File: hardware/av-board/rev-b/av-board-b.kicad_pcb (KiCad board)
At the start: 4 copper layers, 94.6 x 69.4 mm, 234 parts, among them J1 RCA Y, J10 2x20 socket, J11 XIAO 5V..D7, J12 XIAO D0..D6, J13 SPDIF, J2 RCA Pb, J3 RCA Pr, J4 RCA L, J5 RCA R, J6 HDMI-001, J7 SYNC, J8 VGA, J9 2x20 socket, Q1 2N7002, Q2 2N7002, SW1 TS-1187A-B-A-B, SW2 TS-1187A-B-A-B, U1 ADV7181DBCPZ-RL, U10 TPD4E05U06DQAR, U12 TPS7A2045PDBVR, U13 SN74LVC1GU04DBVR, U14 SN74LVC1G04DBVR, U15 SN74LVC1G04DBVR, U19 TPD4E05U06DQAR, U2 ADV7511KSTZ, U20 TPD4E05U06DQAR, U21 SN74LVC2G17DBVR, U22 SN74LVC8T245PWR, U23 SN74AVC4T245PWR, U3 PCM1808PWR, U4 TLV62569DBVR, U5 TPS7A7001DDAR, U6 TPS7A7001DDAR, U7 TPS7A7001DDAR, U8 TPD4E05U06DQAR, U9 TPD4E05U06DQAR, Y1 28.63636MHz 20pF

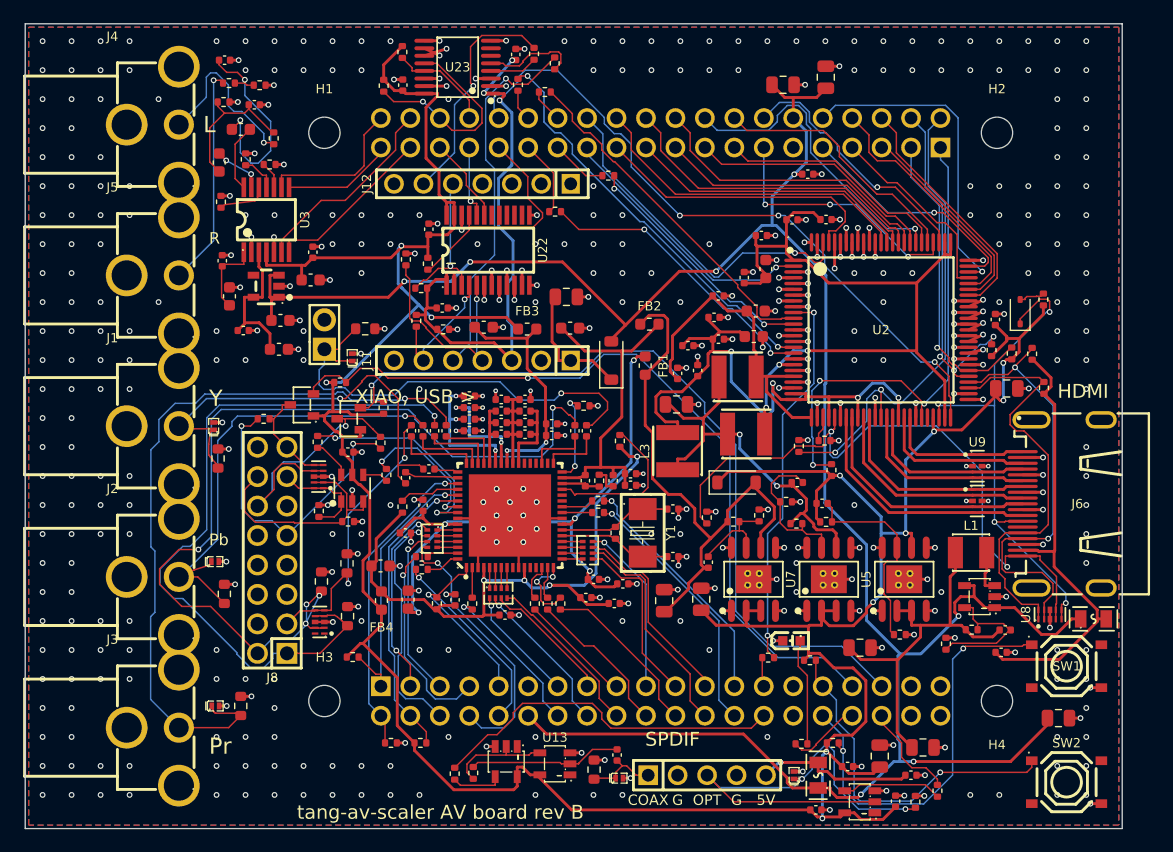
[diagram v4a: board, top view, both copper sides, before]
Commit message: AV boards: rev B, C-B routed on the fixed placement; prune side-by-side copies; JLC jack rotation
Every revision: schematic = board.py, the board = its schematic part for part,
ERC and DRC clean, no unconnected items; rev B's, C-A's and C-B's review tables
measured on these routes.

- Rev B: routed on the capacitor placement fixes (try-b-r1, its last gap
  finished); schematic regenerated (eight capacitors renumbered).
- C-B: the 1V1 buck's inductor and output capacitor placed before its feedback
  divider: in the 3V6 bucks' order the divider's 6.8 pF took the inductor's place
  beside SW, the inductor went above the chip with its SW pad turned away (10.7 mm
  of SW track, FB's copper 0.2 mm from it). Routed again (try-cb-q3): SW 4.1 mm,
  FB 3.0 mm from it; nothing digital within 0.5 mm of an analog line but XTAL1
  beside LLC at the pins' pitch.
- C-A: its review column measured on the route; CPL jack rotations.
- kit/pcbkit.py prune: copper laid side by side taken up too (beside(): the
  shorter of each kit/doubled.py pair), every candidate checked by DRC on a copy
  of the file's text first (save_without(), removable()), so nothing taken out of
  a pcbnew board is put back; rounds run with faulthandler and report a crash's
  signal (one round had segfaulted in libstdc++ with no message).
- kit/pcbkit.py finish_unconnected: a gap's three nearest pad pairs tried in turn
  (rev B's TX_PLVDD pin 21 was walled in towards pin 26, not towards its own
  capacitor).
- kit/gen_fab.py JLC_TURN: JLCPCB places a part by its own footprint for the LCSC
  number; for RCJ-014 and RCJ-017 that is ours turned 90 degrees, so the CPL
  turns those jacks back (their preview had the barrels along the board edge).
  RCJ-012 has no footprint there and is placed as drawn.

Co-Authored-By: Claude Opus 5.5 <noreply@anthropic.com>
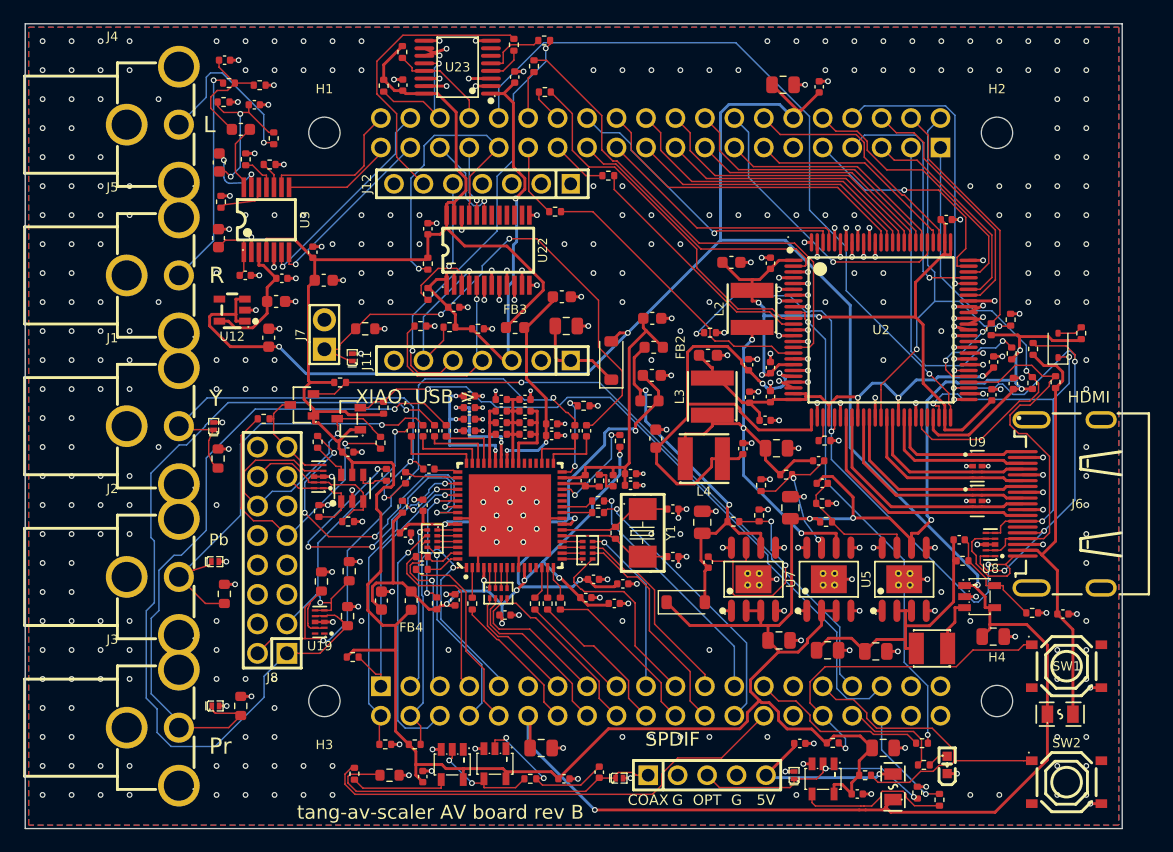
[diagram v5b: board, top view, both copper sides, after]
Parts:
- C10: value 10u -> 6.8p; footprint Capacitor_SMD:C_0805_2012Metric -> Capacitor_SMD:C_0402_1005Metric
- C11: value 6.8p -> 10u; footprint Capacitor_SMD:C_0402_1005Metric -> Capacitor_SMD:C_0805_2012Metric
- C13, C16, C19: value 10u -> 220p; footprint Capacitor_SMD:C_0805_2012Metric -> Capacitor_SMD:C_0402_1005Metric
- C14, C17, C20: value 220p -> 10u; footprint Capacitor_SMD:C_0402_1005Metric -> Capacitor_SMD:C_0805_2012Metric
- moved C2 62.8 mm to (118.7, 83.1), turned to 0 degrees
- moved C76 36.6 mm to (108.5, 85.5), turned to 90 degrees
- moved C21 28.6 mm to (128.2, 50.9), turned to 0 degrees
- moved C88 26.4 mm to (157.7, 49.8), turned to 90 degrees
- moved C83 23.6 mm to (157.6, 52.6)
- moved C75 21.9 mm to (120.7, 85.7)
- moved R74 21.3 mm to (159.2, 46.1)
- moved R73 18.9 mm to (161.0, 51.6)
- moved C13 17.9 mm to (142.9, 60.2)
- moved R60 17.6 mm to (105.6, 85.4), turned to 0 degrees
- moved D2 17.2 mm to (153.7, 84.5), turned to 90 degrees
- moved R77 15.9 mm to (133.3, 47.2), turned to 0 degrees
- moved R69 15.2 mm to (151.5, 82.6)
- moved C80 14.0 mm to (128.6, 56.4), turned to 90 degrees
- moved C19 13.2 mm to (142.6, 58.3)
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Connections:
- C10 pad 2: GND -> FB_3V6
- C11 pad 2: FB_3V6 -> GND
- C13 pad 2: GND -> FB_3V3
- C14 pad 2: FB_3V3 -> GND
- C16 pad 2: GND -> FB_1V8A
- C17 pad 2: FB_1V8A -> GND
- C19 pad 2: GND -> FB_1V8B
- C20 pad 2: FB_1V8B -> GND
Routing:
- net SPDIF_COAX: track 6.41 -> 30.6 mm
- net VGA_G: track 79.7 -> 56.8 mm, vias 5 -> 2
- net SPDIF_OPT: track 40.6 -> 21.3 mm
- net TX_PLVDD: track 27.8 -> 46.0 mm, vias 0 -> 2
- net VGA_VSIN: track 11.9 -> 29.0 mm, vias 2 -> 4
- net VGA_R: track 61.8 -> 76.4 mm
- net 1V8A: track 47.3 -> 33.6 mm, vias 0 -> 2
- net OUT_SPDIF: track 2.53 -> 15.5 mm
- net FB_1V8A: track 8.08 -> 21.0 mm, vias 0 -> 2
- net TX_AVDD: track 51.5 -> 38.6 mm, vias 4 -> 3
- net VGA_HSIN: track 19.0 -> 30.6 mm, vias 2 -> 4
- net SPDIF_RX: track 30.9 -> 41.8 mm
- net HDMI_CEC: track 44.7 -> 34.2 mm, vias 4 -> 3
- net HDMI_SCL: track 36.2 -> 45.8 mm, vias 0 -> 4
- net AUD_DIV_R: track 19.5 -> 10.4 mm, vias 2 -> 0
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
